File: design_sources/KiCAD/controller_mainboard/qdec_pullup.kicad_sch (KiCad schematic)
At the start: 5 parts, among them J12 01x04_JST_PH

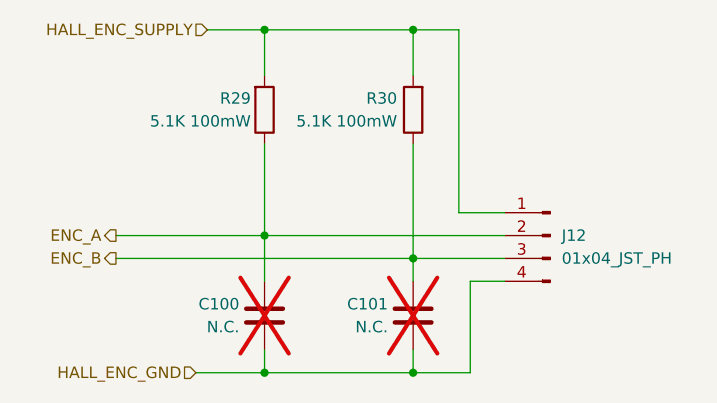
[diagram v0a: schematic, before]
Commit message: Added ESD protection ic, added footprints to all IC and loaded into pcbnew to size up the pcb size.
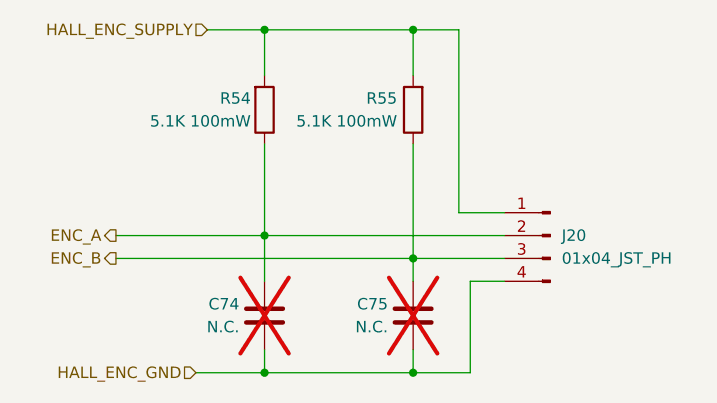
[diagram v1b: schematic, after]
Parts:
- renumbered C100 to C74, C101 to C75, J12 to J20, R29 to R54, R30 to R55
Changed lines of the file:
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@@
 		(dnp no)
 		(fields_autoplaced yes)
-		(property "Reference" "J12"
+		(property "Reference" "J20"
 			(at 166.37 82.5499 0)
 			(effects
@@
 			(project "controller_mainboard"
 				(path "/0fdfffec-3d24-4249-8ba9-dae7a6ccc250/3f02f6d1-4285-41df-89d7-e2f760c4464b"
-					(reference "J19")
+					(reference "J22")
 					(unit 1)
 				)
 				(path "/0fdfffec-3d24-4249-8ba9-dae7a6ccc250/5d34fd63-7af8-4ae6-b870-18314997ed2d"
+					(reference "J23")
+					(unit 1)
+				)
+				(path "/0fdfffec-3d24-4249-8ba9-dae7a6ccc250/8d908822-a6d6-454c-87d0-3d06a8358d54"
 					(reference "J20")
 					(unit 1)
 				)
-				(path "/0fdfffec-3d24-4249-8ba9-dae7a6ccc250/8d908822-a6d6-454c-87d0-3d06a8358d54"
-					(reference "J12")
-					(unit 1)
-				)
 				(path "/0fdfffec-3d24-4249-8ba9-dae7a6ccc250/cc3d023a-c327-49cc-b30a-c3244c45fc4b"
-					(reference "J16")
+					(reference "J21")
 					(unit 1)
 				)
@@
 		(on_board yes)
 		(dnp no)
-		(property "Reference" "R29"
+		(property "Reference" "R54"
 			(at 131.826 67.31 0)
 			(effects
@@
 			(project "controller_mainboard"
 				(path "/0fdfffec-3d24-4249-8ba9-dae7a6ccc250/3f02f6d1-4285-41df-89d7-e2f760c4464b"
-					(reference "R33")
+					(reference "R58")
 					(unit 1)
 				)
 				(path "/0fdfffec-3d24-4249-8ba9-dae7a6ccc250/5d34fd63-7af8-4ae6-b870-18314997ed2d"
-					(reference "R34")
+					(reference "R60")
 					(unit 1)
 				)
 				(path "/0fdfffec-3d24-4249-8ba9-dae7a6ccc250/8d908822-a6d6-454c-87d0-3d06a8358d54"
-					(reference "R29")
+					(reference "R54")
 					(unit 1)
 				)
 				(path "/0fdfffec-3d24-4249-8ba9-dae7a6ccc250/cc3d023a-c327-49cc-b30a-c3244c45fc4b"
-					(reference "R31")
+					(reference "R56")
 					(unit 1)
 				)
@@
 		(on_board yes)
 		(dnp no)
-		(property "Reference" "R30"
+		(property "Reference" "R55"
 			(at 148.082 67.31 0)
 			(effects
@@
 			(project "controller_mainboard"
 				(path "/0fdfffec-3d24-4249-8ba9-dae7a6ccc250/3f02f6d1-4285-41df-89d7-e2f760c4464b"
-					(reference "R35")
+					(reference "R59")
 					(unit 1)
 				)
 				(path "/0fdfffec-3d24-4249-8ba9-dae7a6ccc250/5d34fd63-7af8-4ae6-b870-18314997ed2d"
-					(reference "R68")
+					(reference "R61")
 					(unit 1)
 				)
 				(path "/0fdfffec-3d24-4249-8ba9-dae7a6ccc250/8d908822-a6d6-454c-87d0-3d06a8358d54"
-					(reference "R30")
+					(reference "R55")
 					(unit 1)
 				)
 				(path "/0fdfffec-3d24-4249-8ba9-dae7a6ccc250/cc3d023a-c327-49cc-b30a-c3244c45fc4b"
-					(reference "R32")
+					(reference "R57")
 					(unit 1)
 				)
@@
 		(on_board yes)
 		(dnp yes)
-		(property "Reference" "C101"
+		(property "Reference" "C75"
 			(at 147.066 90.17 0)
 			(effects
@@
 			(project "controller_mainboard"
 				(path "/0fdfffec-3d24-4249-8ba9-dae7a6ccc250/3f02f6d1-4285-41df-89d7-e2f760c4464b"
-					(reference "C106")
+					(reference "C79")
 					(unit 1)
 				)
 				(path "/0fdfffec-3d24-4249-8ba9-dae7a6ccc250/5d34fd63-7af8-4ae6-b870-18314997ed2d"
-					(reference "C107")
+					(reference "C81")
 					(unit 1)
 				)
 				(path "/0fdfffec-3d24-4249-8ba9-dae7a6ccc250/8d908822-a6d6-454c-87d0-3d06a8358d54"
-					(reference "C101")
+					(reference "C75")
 					(unit 1)
 				)
 				(path "/0fdfffec-3d24-4249-8ba9-dae7a6ccc250/cc3d023a-c327-49cc-b30a-c3244c45fc4b"
-					(reference "C103")
+					(reference "C77")
 					(unit 1)
 				)
@@
 		(on_board yes)
 		(dnp yes)
-		(property "Reference" "C100"
+		(property "Reference" "C74"
 			(at 130.556 90.17 0)
 			(effects
@@
 			(project "controller_mainboard"
 				(path "/0fdfffec-3d24-4249-8ba9-dae7a6ccc250/3f02f6d1-4285-41df-89d7-e2f760c4464b"
-					(reference "C104")
+					(reference "C78")
 					(unit 1)
 				)
 				(path "/0fdfffec-3d24-4249-8ba9-dae7a6ccc250/5d34fd63-7af8-4ae6-b870-18314997ed2d"
-					(reference "C105")
+					(reference "C80")
 					(unit 1)
 				)
 				(path "/0fdfffec-3d24-4249-8ba9-dae7a6ccc250/8d908822-a6d6-454c-87d0-3d06a8358d54"
-					(reference "C100")
+					(reference "C74")
 					(unit 1)
 				)
 				(path "/0fdfffec-3d24-4249-8ba9-dae7a6ccc250/cc3d023a-c327-49cc-b30a-c3244c45fc4b"
-					(reference "C102")
-					(unit 1)
-				)
+					(reference "C76")
+					(unit 1)
+				)

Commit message: Changed JLCPCB field to LCSC
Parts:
- R54, R55: JLCPCB C23186 -> (none); LCSC (none) -> C23186
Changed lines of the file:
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@@
 			)
 		)
-		(property "JLCPCB" "C23186"
+		(property "LCSC" "C23186"
 			(at 133.35 68.58 0)
 			(effects
@@
 			)
 		)
-		(property "JLCPCB" "C23186"
+		(property "LCSC" "C23186"
 			(at 149.86 68.58 0)
 			(effects
@@
 			)
 		)
-		(property "JLCPCB" ""
-			(at 149.86 91.44 0)
-			(effects
-				(font
-					(size 1.27 1.27)
-				)
-				(hide yes)
-			)
-		)
 		(pin "1"
 		)
@@
 			(at 133.35 91.44 0)
 			(effects
-				(font
-					(size 1.27 1.27)
-				)
-				(hide yes)
-			)
-		)
-		(property "JLCPCB" ""
-			(at 133.35 91.44 0)
-			(effects
